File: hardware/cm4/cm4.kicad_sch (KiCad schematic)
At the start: 15 parts, among them J11 CM4 Stecker 1, J12 CM4 Stecker 2, M1 Raspberry Pi CM4 (z. B. CM410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, Q10 BSS84

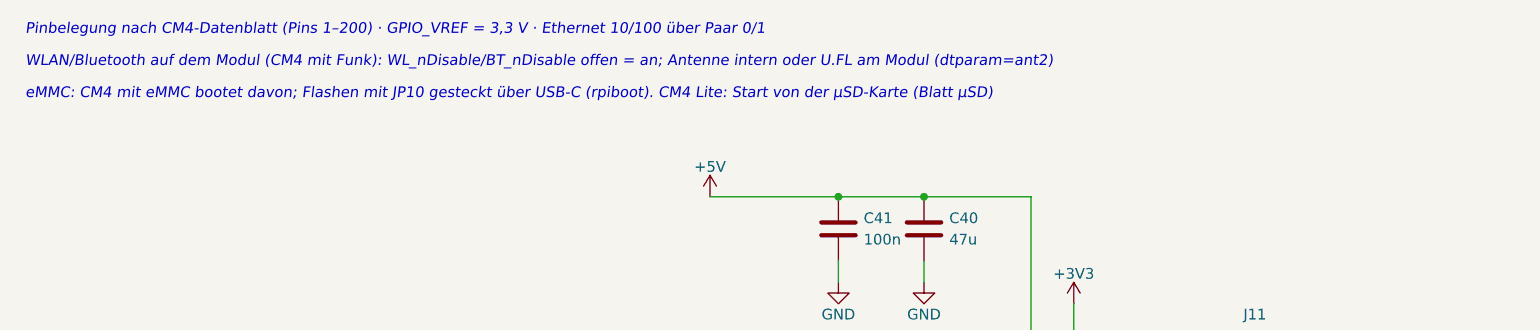
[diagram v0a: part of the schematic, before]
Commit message: Schaltplan: Hinweise als Textkästen (KiCad bricht um); Texte werden in den Generator zurückgeführt
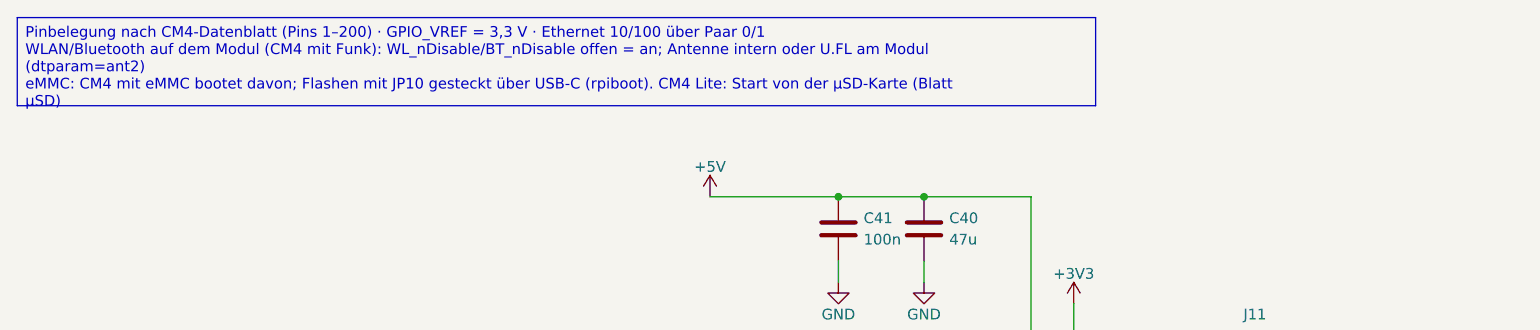
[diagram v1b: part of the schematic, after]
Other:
- note removed: "Pinbelegung nach CM4-Datenblatt (Pins 1–200) · GPIO_VREF = 3,3 V · Ethernet 10/100 über Paar 0/1"
- note removed: "WLAN/Bluetooth auf dem Modul (CM4 mit Funk): WL_nDisable/BT_nDisable offen = an; Antenne intern oder U.FL am Modul (dtparam=ant2)"
- note removed: "eMMC: CM4 mit eMMC bootet davon; Flashen mit JP10 gesteckt über USB-C (rpiboot). CM4 Lite: Start von der µSD-Karte (Blatt µSD)"
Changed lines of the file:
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@@
 	(text "H5–H8: Bohrungen des CM4 (Abstandsbolzen M2,5, Raster 48 × 33 mm)" (exclude_from_sim no) (at 288.19 214.41 0) (effects (font (size 1.27 1.27) italic) (justify left bottom)))
 	(text "M1: das CM4 selbst (Platzhalter für Stückliste und 3D-Ansicht, gesteckt, nicht bestückt)" (exclude_from_sim no) (at 288.19 241.41 0) (effects (font (size 1.27 1.27) italic) (justify left bottom)))
-	(text "Pinbelegung nach CM4-Datenblatt (Pins 1–200) · GPIO_VREF = 3,3 V · Ethernet 10/100 über Paar 0/1" (exclude_from_sim no) (at 31.75 24.13 0) (effects (font (size 1.27 1.27) italic) (justify left bottom)))
-	(text "WLAN/Bluetooth auf dem Modul (CM4 mit Funk): WL_nDisable/BT_nDisable offen = an; Antenne intern oder U.FL am Modul (dtparam=ant2)" (exclude_from_sim no) (at 31.75 27.94 0) (effects (font (size 1.27 1.27) italic) (justify left bottom)))
-	(text "eMMC: CM4 mit eMMC bootet davon; Flashen mit JP10 gesteckt über USB-C (rpiboot). CM4 Lite: Start von der µSD-Karte (Blatt µSD)" (exclude_from_sim no) (at 31.75 31.75 0) (effects (font (size 1.27 1.27) italic) (justify left bottom)))
+	(text_box "Pinbelegung nach CM4-Datenblatt (Pins 1–200) · GPIO_VREF = 3,3 V · Ethernet 10/100 über Paar 0/1\nWLAN/Bluetooth auf dem Modul (CM4 mit Funk): WL_nDisable/BT_nDisable offen = an; Antenne intern oder U.FL am Modul (dtparam=ant2)\neMMC: CM4 mit eMMC bootet davon; Flashen mit JP10 gesteckt über USB-C (rpiboot). CM4 Lite: Start von der µSD-Karte (Blatt µSD)" (exclude_from_sim no) (at 30.8 21.91 0) (size 128 10.46) (margins 0.9525 0.9525 0.9525 0.9525) (stroke (width 0.1) (type solid) (color 132 132 132 1)) (fill (type color) (color 255 255 230 1)) (effects (font (size 1.27 1.27)) (justify left top)))
 	(embedded_fonts no)
 )

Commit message: CM4-Schaltplan: Handänderungen übernommen (Handlage für 8 Blätter, 2 Texte zurückgeführt); Kastenhöhen aus gemessenen Zeichenbreiten
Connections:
- no-connect marks 107 -> 105
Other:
- moved on the sheet: H5, H6, H7, H8, M1
